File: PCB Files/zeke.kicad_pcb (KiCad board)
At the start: 2 copper layers, 78.6 x 120.3 mm, 135 parts, among them J1 USB_C, SW1 MXSwitch, SW10 MXSwitch, SW11 MXSwitch, SW12 MXSwitch, SW13 MXSwitch, SW14 MXSwitch, SW15 MXSwitch, SW16 MXSwitch, SW17 MXSwitch, SW18 MXSwitch, SW19 MXSwitch, SW2 MXSwitch, SW20 MXSwitch, SW21 MXSwitch, SW22 MXSwitch, SW23 MXSwitch, SW24 MXSwitch, SW25 MXSwitch, SW26 MXSwitch, SW27 MXSwitch, SW3 MXSwitch, SW4 MXSwitch, SW5 MXSwitch, SW6 MXSwitch, SW7 MXSwitch, SW8 MXSwitch, SW9 MXSwitch, U1 WS2811M, U10 WS2811M, U11 WS2811M, U12 WS2811M, U13 WS2811M, U14 WS2811M, U15 WS2811M, U16 WS2811M, U17 WS2811M, U18 WS2811M, U19 WS2811M, U2 WS2811M, U20 WS2811M, U21 WS2811M, U22 WS2811M, U23 WS2811M, U24 WS2811M, U28 USBLC6-2SC6, U29 ATMEGA32U4, U3 WS2811M, U4 WS2811M, U5 WS2811M, U6 WS2811M, U7 WS2811M, U8 WS2811M, U9 WS2811M, X1 16MHz

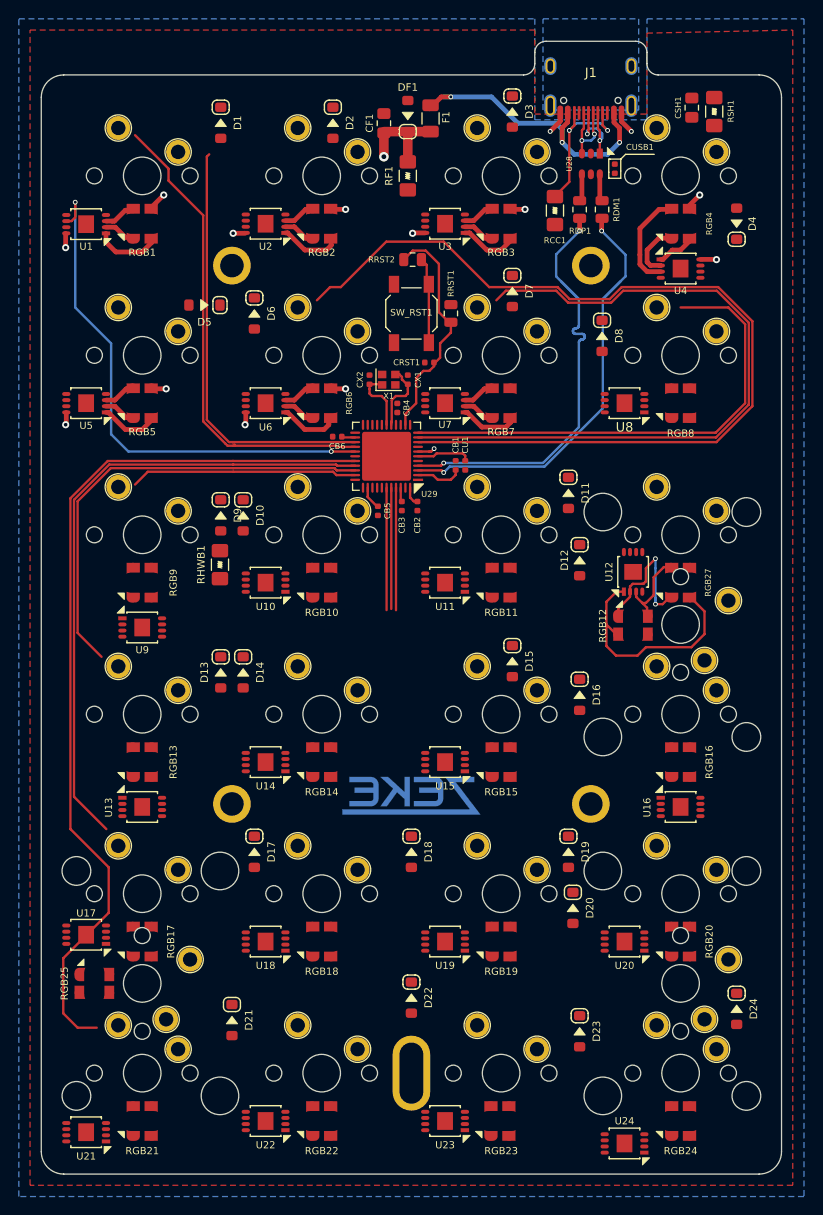
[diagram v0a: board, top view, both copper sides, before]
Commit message: [Update] Added new footprint for the RGB LEDs with the 3D model, added Acheron Short logo
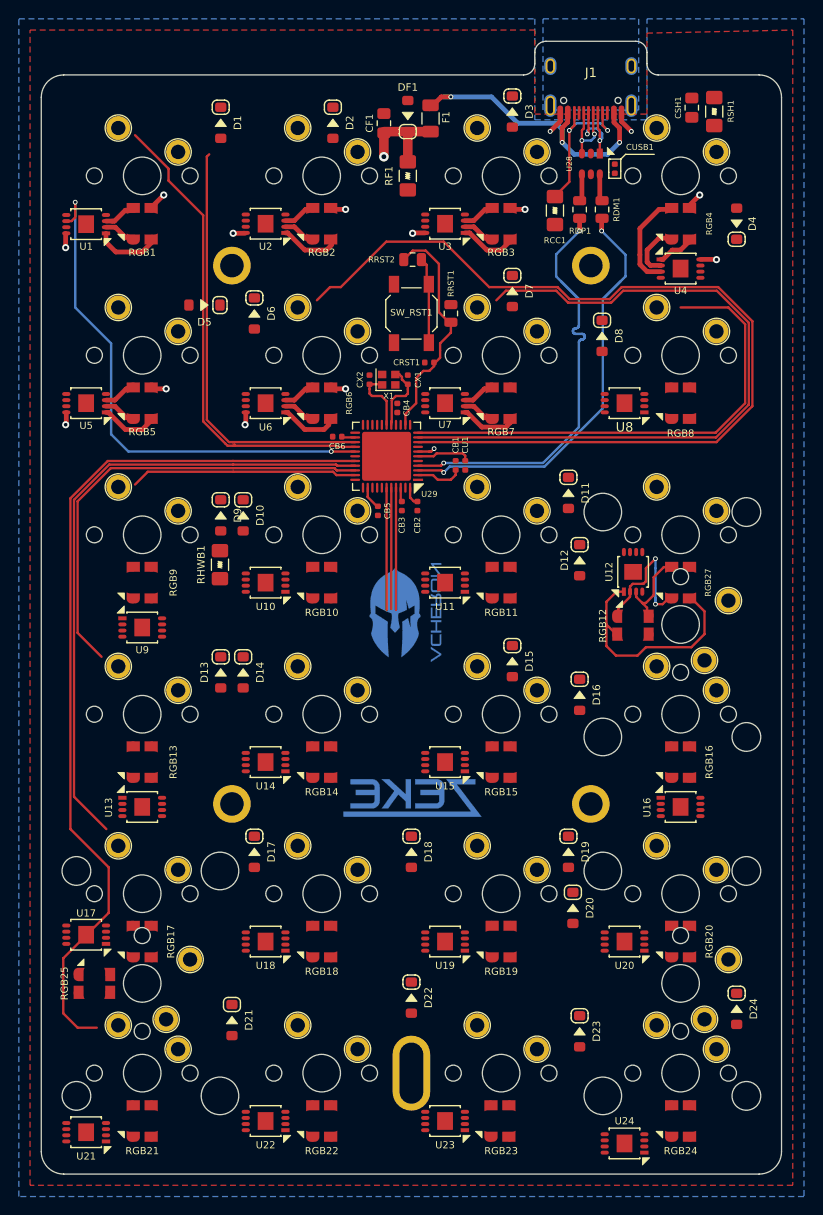
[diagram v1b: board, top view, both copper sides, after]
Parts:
- removed G***: LOGO, zekeGraphics:zekeLogo
- added L1: Zeke Logo, zekeGraphics:zekeLogo, B.Cu at (75.1, 112.5)
- added L2: Acheron Short Logo Plated, acheron_Logos:acheronShort_0.3x0.5in_Plated, B.Cu at (74.4, 92.8)
